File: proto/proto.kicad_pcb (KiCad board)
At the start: 2 copper layers, 12 parts, among them J1 Conn_01x10_Pin, U2 TPIC6595

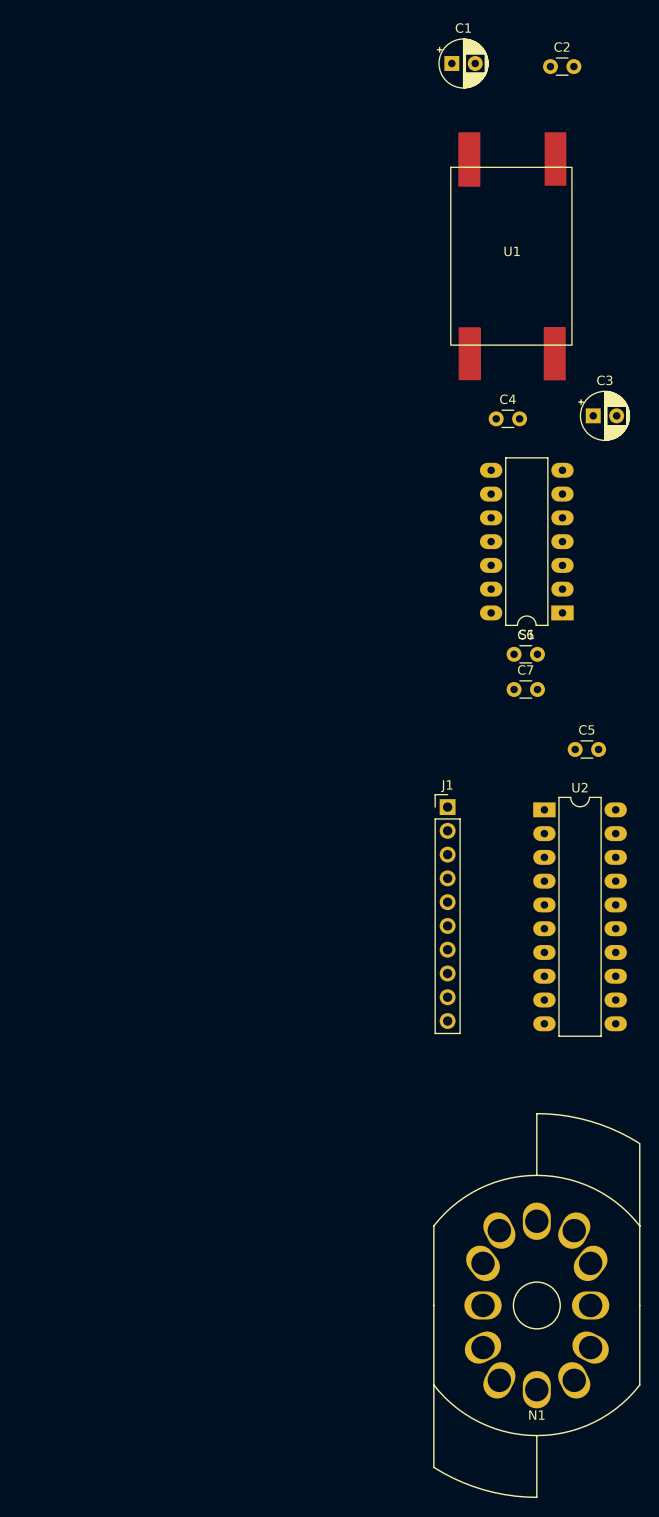
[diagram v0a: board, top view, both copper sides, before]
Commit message: Add footprint for socketed HV supply. Add R1 which was forgotten. Revise layout for significantly better density.
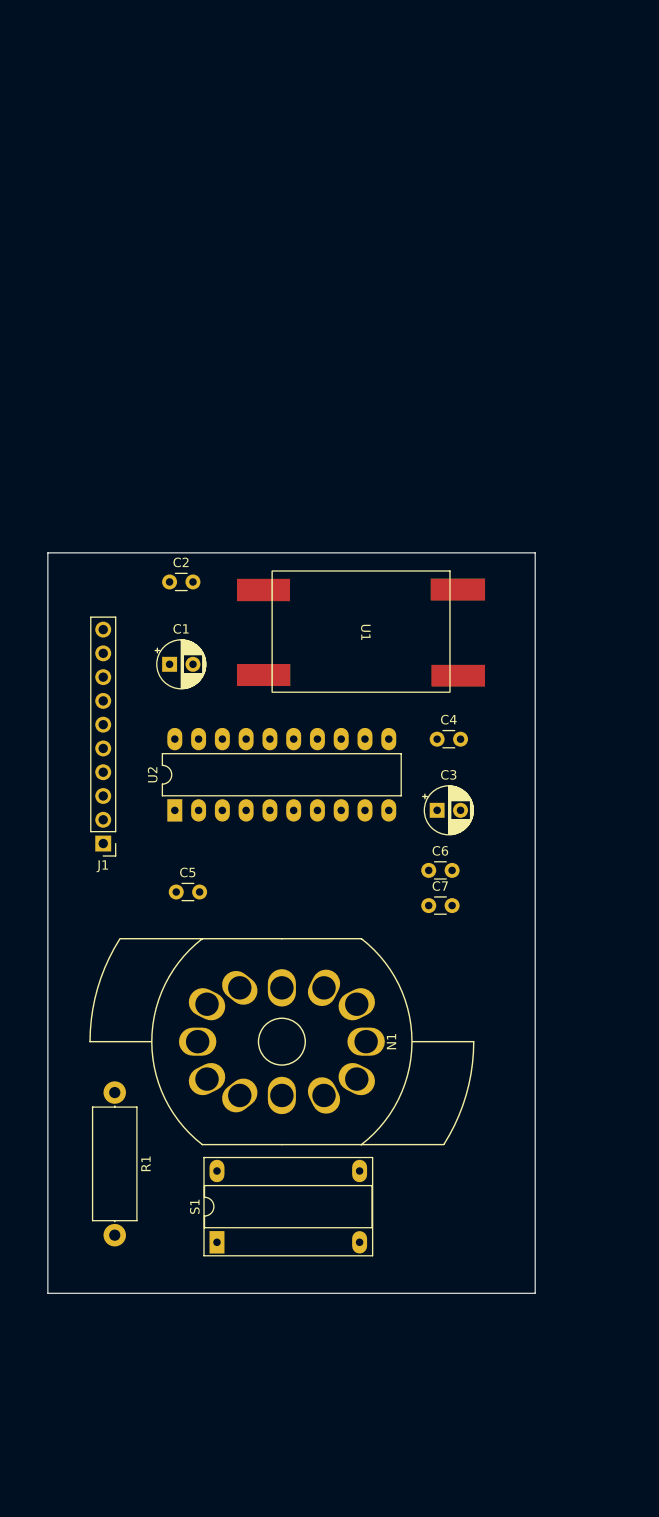
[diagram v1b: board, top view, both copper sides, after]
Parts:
- added R1: R, Resistor_THT:R_Axial_DIN0414_L11.9mm_D4.5mm_P15.24mm_Horizontal, F.Cu at (89.8, 149.2)
- S1: footprint Package_DIP:DIP-14_W7.62mm_LongPads -> NixComp:NCH8200HV_Socket_LongPads
- moved S1 76.7 mm to (100.7, 165.2), turned to 90 degrees
- moved C1 70.9 mm to (95.7, 103.4)
- moved C2 68.5 mm to (95.7, 94.6)
- moved C3 45.3 mm to (124.2, 119.0)
- moved C5 45.3 mm to (96.4, 127.8)
- moved U1 43.3 mm to (116.1, 100.0), turned to -90 degrees
- moved U2 39.5 mm to (96.2, 119.0), turned to 90 degrees
- moved N1 39.2 mm to (107.7, 143.8), turned to 90 degrees
- moved J1 37.0 mm to (88.6, 122.6), turned to 180 degrees
- moved C4 34.8 mm to (124.2, 111.4)
- moved C6 24.8 mm to (123.3, 125.5)
- moved C7 24.8 mm to (123.3, 129.2)
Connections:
- S1 pad 4: Net-(N1-A) -> Net-(S1-HV_OUT)
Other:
- board outline added: 52.1 x 79.1 mm

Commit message: Ongoing development
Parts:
- added J2: Conn_01x05_Pin, Connector_PinHeader_2.54mm:PinHeader_1x05_P2.54mm_Vertical, F.Cu at (132.3, 126.0)
- added J3: Conn_01x05_Pin, Connector_PinHeader_2.54mm:PinHeader_1x05_P2.54mm_Vertical, F.Cu at (84.5, 125.9)
- added J4: Conn_01x05_Pin, Connector_PinHeader_2.54mm:PinHeader_1x05_P2.54mm_Vertical, F.Cu at (129.8, 126.0)
- added J5: Conn_01x05_Pin, Connector_PinHeader_2.54mm:PinHeader_1x05_P2.54mm_Vertical, F.Cu at (87.1, 125.9)
- moved C3 6.54 mm to (129.4, 115.0)
- moved U2 6.30 mm to (102.1, 116.9)
- moved C4 5.78 mm to (129.4, 108.8)
- moved N1 4.47 mm to (111.6, 145.9)
- moved J1 4.11 mm to (92.6, 122.0)
- moved R1 2.68 mm to (89.7, 151.9)
- moved S1 1.85 mm to (100.6, 167.0)
- moved C1 1.43 mm to (96.9, 102.8)
- moved C2 1.26 mm to (96.8, 95.0)
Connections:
- C1 pad 1: Net-(J1-Pin_10) -> Net-(J2-Pin_1)
- C2 pad 1: Net-(J1-Pin_10) -> Net-(J2-Pin_1)
- C3 pad 1: Net-(S1-LV_IN) -> Net-(J5-Pin_1)
- C4 pad 1: Net-(S1-LV_IN) -> Net-(J5-Pin_1)
- C5 pad 1: Net-(J1-Pin_10) -> Net-(J2-Pin_1)
- C6 pad 1: Net-(J1-Pin_10) -> Net-(J5-Pin_1)
- C7 pad 1: Net-(J1-Pin_10) -> Net-(J5-Pin_1)
- J1 pad 10: Net-(J1-Pin_10) -> unconnected-(J1-Pin_10-Pad10)
- J1 pad 2: Net-(J1-Pin_2) -> unconnected-(J1-Pin_2-Pad2)
- J1 pad 5: Net-(J1-Pin_5) -> unconnected-(J1-Pin_5-Pad5)
- J1 pad 6: unconnected-(J1-Pin_6-Pad6) -> Net-(J1-Pin_6)
- J1 pad 7: unconnected-(J1-Pin_7-Pad7) -> Net-(J1-Pin_7)
- J1 pad 9: Net-(J1-Pin_10) -> unconnected-(J1-Pin_9-Pad9)
- S1 pad 1: Net-(S1-LV_IN) -> Net-(J5-Pin_1)
- U1 pad 1: Net-(J1-Pin_10) -> Net-(J2-Pin_1)
- U1 pad 2: Net-(S1-LV_IN) -> Net-(J5-Pin_1)
- U2 pad 12: Net-(J1-Pin_4) -> Net-(J1-Pin_6)
- U2 pad 13: Net-(J1-Pin_2) -> Net-(J1-Pin_3)
- U2 pad 2: Net-(S1-LV_IN) -> Net-(J5-Pin_1)
- U2 pad 8: Net-(J1-Pin_3) -> Net-(J1-Pin_4)
- U2 pad 9: Net-(J1-Pin_5) -> Net-(J1-Pin_7)
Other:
- board size 52.1 x 79.1 mm -> 52.7 x 79.1 mm
- copper layers 2 -> 4

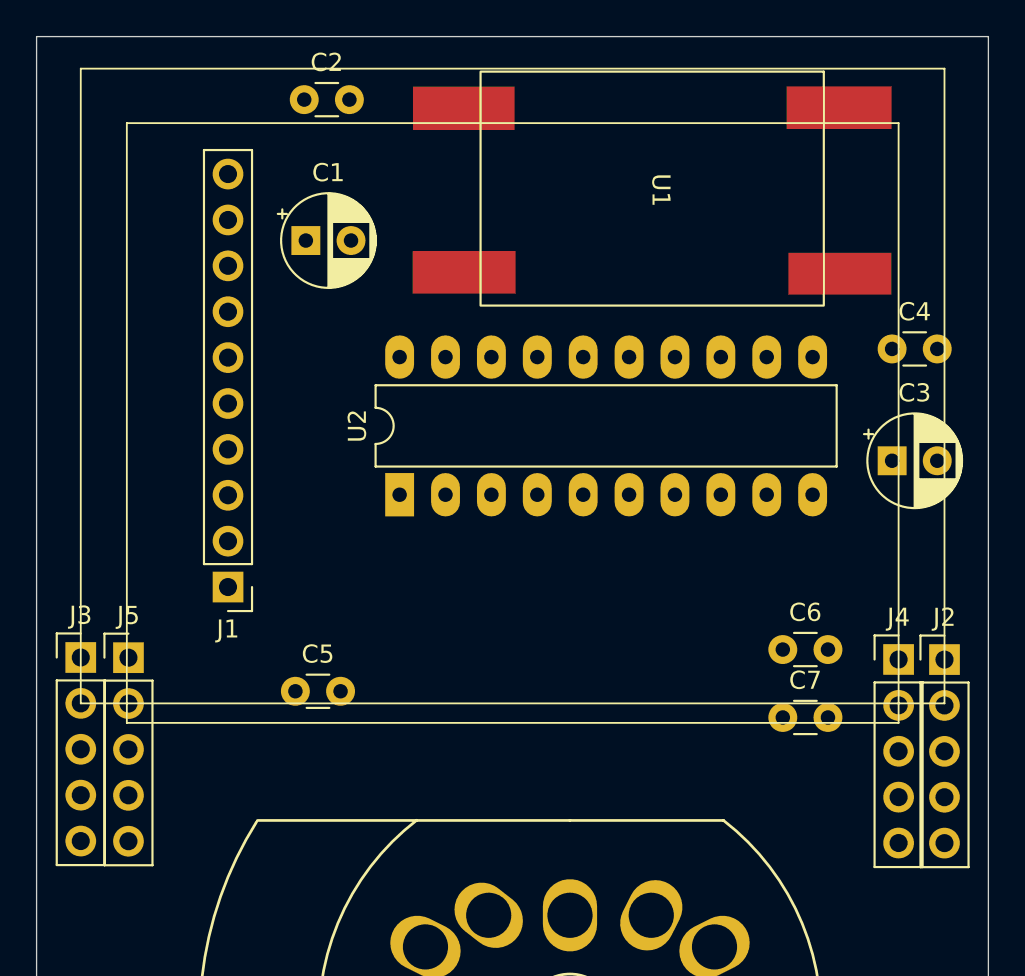
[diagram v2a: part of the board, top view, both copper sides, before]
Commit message: Improve footprint for pin connectors and align four power and ground connectors (I hope)
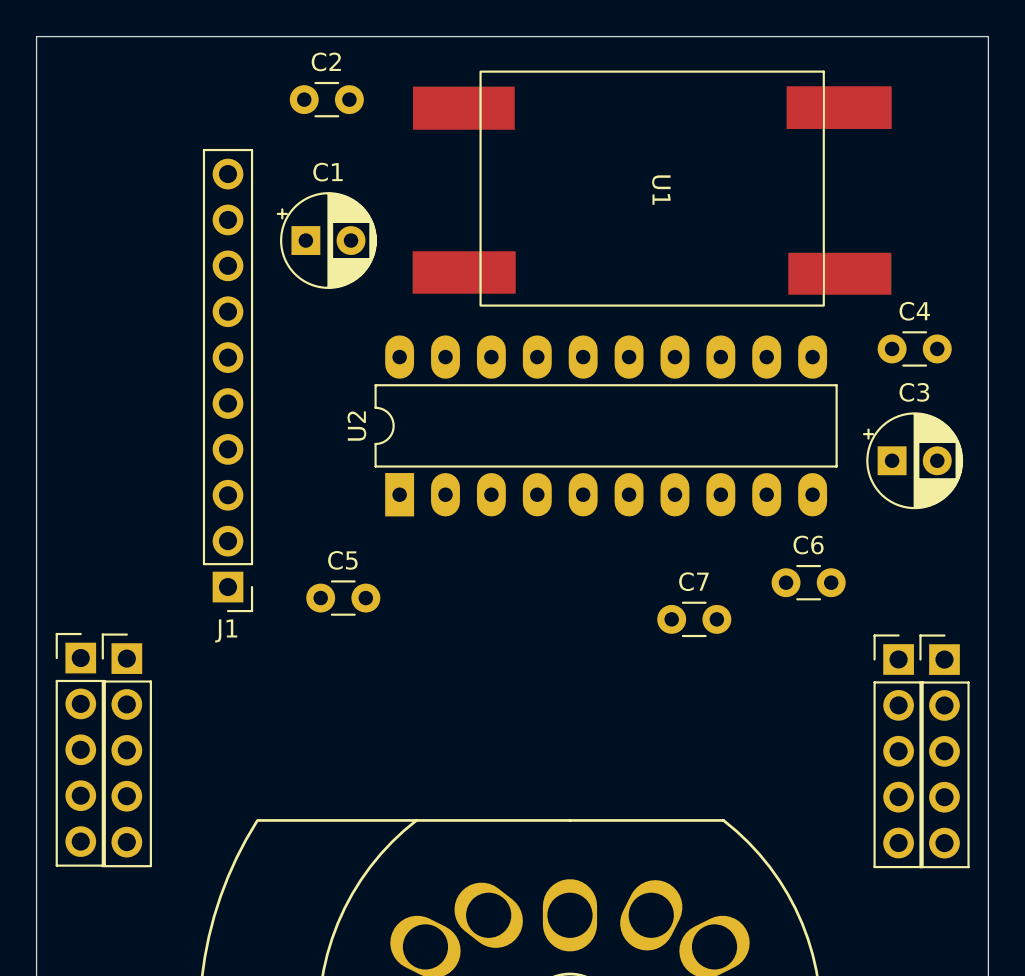
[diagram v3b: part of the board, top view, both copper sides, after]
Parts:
- J2, J3, J4, J5: footprint Connector_PinHeader_2.54mm:PinHeader_1x05_P2.54mm_Vertical -> NixComp:PinHeader_1x05_P2.54mm_Vertical_SmallCourt
- moved C7 8.20 mm to (117.2, 123.8)
- moved C5 5.35 mm to (97.8, 122.6)
- moved C6 3.70 mm to (123.5, 121.8)
- moved J5 0.10 mm to (87.0, 126.0)
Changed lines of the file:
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@@
 		)
 	)
-	(footprint "Connector_PinHeader_2.54mm:PinHeader_1x05_P2.54mm_Vertical"
+	(footprint "NixComp:PinHeader_1x05_P2.54mm_Vertical_SmallCourt"
 		(layer "F.Cu")
 		(at 132.29 126.005)
@@
 		(tags "Through hole pin header THT 1x05 2.54mm single row")
 		(property "Reference" "J2"
-			(at 0 -2.33 0)
+			(at -0.03 -2.43 0)
 			(layer "F.SilkS")
+			(hide yes)
 			(effects
 				(font
@@
 			)
 		)
-		(property "Footprint" "Connector_PinHeader_2.54mm:PinHeader_1x05_P2.54mm_Vertical"
+		(property "Footprint" "NixComp:PinHeader_1x05_P2.54mm_Vertical_SmallCourt"
 			(at 0 0 0)
 			(unlocked yes)
@@
 		)
 		(fp_line
-			(start -1.8 -1.8)
-			(end -1.8 11.95)
-			(stroke
-				(width 0.05)
-				(type solid)
-			)
-			(layer "F.CrtYd")
-		)
-		(fp_line
-			(start -1.8 11.95)
-			(end 1.8 11.95)
-			(stroke
-				(width 0.05)
-				(type solid)
-			)
-			(layer "F.CrtYd")
-		)
-		(fp_line
-			(start 1.8 -1.8)
-			(end -1.8 -1.8)
-			(stroke
-				(width 0.05)
-				(type solid)
-			)
-			(layer "F.CrtYd")
-		)
-		(fp_line
-			(start 1.8 11.95)
-			(end 1.8 -1.8)
-			(stroke
-				(width 0.05)
-				(type solid)
-			)
-			(layer "F.CrtYd")
-		)
-		(fp_line
 			(start -1.27 -0.635)
 			(end -0.635 -1.27)
@@
 	(footprint "Capacitor_THT:C_Disc_D3.0mm_W1.6mm_P2.50mm"
 		(layer "F.Cu")
-		(at 96.36 127.76)
+		(at 97.76 122.6)
 		(descr "C, Disc series, Radial, pin pitch=2.50mm, , diameter*width=3.0*1.6mm^2, Capacitor, http://www.vishay.com/docs/45233/krseries.pdf")
 		(tags "C Disc series Radial pin pitch 2.50mm  diameter 3.0mm width 1.6mm Capacitor")
@@
 	(footprint "Capacitor_THT:C_Disc_D3.0mm_W1.6mm_P2.50mm"
 		(layer "F.Cu")
-		(at 123.34 125.45)
+		(at 123.52 121.75)
 		(descr "C, Disc series, Radial, pin pitch=2.50mm, , diameter*width=3.0*1.6mm^2, Capacitor, http://www.vishay.com/docs/45233/krseries.pdf")
 		(tags "C Disc series Radial pin pitch 2.50mm  diameter 3.0mm width 1.6mm Capacitor")
@@
 		)
 	)
-	(footprint "Connector_PinHeader_2.54mm:PinHeader_1x05_P2.54mm_Vertical"
+	(footprint "NixComp:PinHeader_1x05_P2.54mm_Vertical_SmallCourt"
 		(layer "F.Cu")
 		(at 129.75 126)
@@
 		(tags "Through hole pin header THT 1x05 2.54mm single row")
 		(property "Reference" "J4"
-			(at 0 -2.33 0)
+			(at -0.03 -2.43 0)
 			(layer "F.SilkS")
+			(hide yes)
 			(effects
 				(font
@@
 			)
 		)
-		(property "Footprint" "Connector_PinHeader_2.54mm:PinHeader_1x05_P2.54mm_Vertical"
+		(property "Footprint" "NixComp:PinHeader_1x05_P2.54mm_Vertical_SmallCourt"
 			(at 0 0 0)
 			(unlocked yes)
@@
 		)
 		(fp_line
-			(start -1.8 -1.8)
-			(end -1.8 11.95)
-			(stroke
-				(width 0.05)
-				(type solid)
-			)
-			(layer "F.CrtYd")
-		)
-		(fp_line
-			(start -1.8 11.95)
-			(end 1.8 11.95)
-			(stroke
-				(width 0.05)
-				(type solid)
-			)
-			(layer "F.CrtYd")
-		)
-		(fp_line
-			(start 1.8 -1.8)
-			(end -1.8 -1.8)
-			(stroke
-				(width 0.05)
-				(type solid)
-			)
-			(layer "F.CrtYd")
-		)
-		(fp_line
-			(start 1.8 11.95)
-			(end 1.8 -1.8)
-			(stroke
-				(width 0.05)
-				(type solid)
-			)
-			(layer "F.CrtYd")
-		)
-		(fp_line
 			(start -1.27 -0.635)
 			(end -0.635 -1.27)
@@
 		)
 	)
-	(footprint "Connector_PinHeader_2.54mm:PinHeader_1x05_P2.54mm_Vertical"
+	(footprint "NixComp:PinHeader_1x05_P2.54mm_Vertical_SmallCourt"
 		(layer "F.Cu")
-		(at 87.12 125.9)
+		(at 87.03 125.95)
 		(descr "Through hole straight pin header, 1x05, 2.54mm pitch, single row")
 		(tags "Through hole pin header THT 1x05 2.54mm single row")
 		(property "Reference" "J5"
-			(at 0 -2.33 0)
+			(at -0.03 -2.43 0)
 			(layer "F.SilkS")
+			(hide yes)
 			(effects
 				(font
@@
 			)
 		)
-		(property "Footprint" "Connector_PinHeader_2.54mm:PinHeader_1x05_P2.54mm_Vertical"
+		(property "Footprint" "NixComp:PinHeader_1x05_P2.54mm_Vertical_SmallCourt"
 			(at 0 0 0)
 			(unlocked yes)
@@
 		)
 		(fp_line
-			(start -1.8 -1.8)
-			(end -1.8 11.95)
-			(stroke
-				(width 0.05)
-				(type solid)
-			)
-			(layer "F.CrtYd")
-		)
-		(fp_line
-			(start -1.8 11.95)
-			(end 1.8 11.95)
-			(stroke
-				(width 0.05)
-				(type solid)
-			)
-			(layer "F.CrtYd")
-		)
-		(fp_line
-			(start 1.8 -1.8)
-			(end -1.8 -1.8)
-			(stroke
-				(width 0.05)
-				(type solid)
-			)
-			(layer "F.CrtYd")
-		)
-		(fp_line
-			(start 1.8 11.95)
-			(end 1.8 -1.8)
-			(stroke
-				(width 0.05)
-				(type solid)
-			)
-			(layer "F.CrtYd")
-		)
-		(fp_line
 			(start -1.27 -0.635)
 			(end -0.635 -1.27)
@@
 	(footprint "Capacitor_THT:C_Disc_D3.0mm_W1.6mm_P2.50mm"
 		(layer "F.Cu")
-		(at 123.34 129.21)
+		(at 117.19 123.78)
 		(descr "C, Disc series, Radial, pin pitch=2.50mm, , diameter*width=3.0*1.6mm^2, Capacitor, http://www.vishay.com/docs/45233/krseries.pdf")
 		(tags "C Disc series Radial pin pitch 2.50mm  diameter 3.0mm width 1.6mm Capacitor")
@@
 		)
 	)
-	(footprint "Connector_PinHeader_2.54mm:PinHeader_1x05_P2.54mm_Vertical"
+	(footprint "NixComp:PinHeader_1x05_P2.54mm_Vertical_SmallCourt"
 		(layer "F.Cu")
-		(at 84.48 125.89)
+		(at 84.48 125.92)
 		(descr "Through hole straight pin header, 1x05, 2.54mm pitch, single row")
 		(tags "Through hole pin header THT 1x05 2.54mm single row")
 		(property "Reference" "J3"
-			(at 0 -2.33 0)
+			(at -0.03 -2.43 0)
 			(layer "F.SilkS")
+			(hide yes)
 			(effects
 				(font
@@
 			)
 		)
-		(property "Footprint" "Connector_PinHeader_2.54mm:PinHeader_1x05_P2.54mm_Vertical"
+		(property "Footprint" "NixComp:PinHeader_1x05_P2.54mm_Vertical_SmallCourt"
 			(at 0 0 0)
 			(unlocked yes)
@@
 		)
 		(fp_line
-			(start -1.8 -1.8)
-			(end -1.8 11.95)
-			(stroke
-				(width 0.05)
-				(type solid)
-			)
-			(layer "F.CrtYd")
-		)
-		(fp_line
-			(start -1.8 11.95)
-			(end 1.8 11.95)
-			(stroke
-				(width 0.05)
-				(type solid)
-			)
-			(layer "F.CrtYd")
-		)
-		(fp_line
-			(start 1.8 -1.8)
-			(end -1.8 -1.8)
-			(stroke
-				(width 0.05)
-				(type solid)
-			)
-			(layer "F.CrtYd")
-		)
-		(fp_line
-			(start 1.8 11.95)
-			(end 1.8 -1.8)
-			(stroke
-				(width 0.05)
-				(type solid)
-			)
-			(layer "F.CrtYd")
-		)
-		(fp_line
 			(start -1.27 -0.635)
 			(end -0.635 -1.27)
@@
 	)
 	(gr_rect
-		(start 87.03 96.31)
-		(end 129.75 129.51)
-		(stroke
-			(width 0.1)
-			(type default)
-		)
-		(fill none)
-		(layer "F.SilkS")
-	)
-	(gr_rect
-		(start 84.48 93.2946)
-		(end 132.29 128.43)
-		(stroke
-			(width 0.1)
-			(type default)
-		)
-		(fill none)
-		(layer "F.SilkS")
-	)
-	(gr_rect
 		(start 82.033846 91.52)
 		(end 134.72 170.643846)
@@
 		(layer "F.SilkS")
 		(pts
-			(xy 132.29 129.59) (xy 129.75 129.59)
-		)
-		(height 0)
-		(gr_text "2.5400 mm"
-			(at 131.02 128.49 0)
-			(layer "F.SilkS")
-			(effects
-				(font
-					(size 1 1)
-					(thickness 0.1)
-				)
-			)
-		)
-		(format
-			(prefix "")
-			(suffix "")
-			(units 3)
-			(units_format 1)
-			(precision 4)
-		)
-		(style
-			(thickness 0.1)
-			(arrow_length 1.27)
-			(text_position_mode 0)
-			(extension_height 0.58642)
-			(extension_offset 0.5) keep_text_aligned)
-	)
-	(dimension
-		(type aligned)
-		(layer "F.SilkS")
-		(pts
 			(xy 108.39 131.081923) (xy 82.06 131.081923)
 		)
@@
 		(layer "F.SilkS")
 		(pts
-			(xy 84.48 129.51) (xy 87.03 129.51)
+			(xy 87.03 126.92) (xy 129.74 126.92)
 		)
 		(height 0)
-		(gr_text "2.5500 mm"
-			(at 85.755 128.41 0)
+		(gr_text "42.7100 mm"
+			(at 108.385 125.82 0)
 			(layer "F.SilkS")
 			(effects

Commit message: Ongoing development. Add ground vias.
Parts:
- J1: value Conn_01x10_Pin -> J1; footprint Connector_PinHeader_2.54mm:PinHeader_1x10_P2.54mm_Vertical -> NixComp:PinHeader_1x05_P2.54mm_Vertical_SmallCourt
- J2: value Conn_01x05_Pin -> J2
- J4: value Conn_01x05_Pin -> J4
- moved J1 15.8 mm to (93.9, 106.2), turned to 0 degrees
- moved C1 10.8 mm to (86.2, 101.3)
- moved C2 10.6 mm to (86.3, 94.8)
- moved U1 3.41 mm to (112.7, 100.3)
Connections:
- J1 pad 2: unconnected-(J1-Pin_2-Pad2) -> Net-(J1-Pin_2)
- J1 pad 5: unconnected-(J1-Pin_5-Pad5) -> Net-(J1-Pin_5)
- U2 pad 12: Net-(J1-Pin_6) -> Net-(J1-Pin_4)
- U2 pad 13: Net-(J1-Pin_3) -> Net-(J1-Pin_2)
- U2 pad 8: Net-(J1-Pin_4) -> Net-(J1-Pin_3)
- U2 pad 9: Net-(J1-Pin_7) -> Net-(J1-Pin_5)
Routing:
- net GND: track 0.00 -> 48.8 mm, vias 0 -> 24
- added copper zone on In1.Cu, net GND
- added copper zone on In2.Cu, net GND

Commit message: Equivalent of code complete on the proto board
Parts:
- J3: value Conn_01x05_Pin -> J3
- J5: value Conn_01x05_Pin -> J5
- moved C2 65.3 mm to (132.3, 141.2), turned to 180 degrees
- moved C4 41.1 mm to (89.5, 99.0), turned to -90 degrees
- moved C1 39.8 mm to (126.0, 99.2), turned to -90 degrees
- moved C5 39.4 mm to (130.0, 99.9), turned to -90 degrees
- moved C6 36.5 mm to (87.1, 122.7), turned to 90 degrees
- moved C3 34.1 mm to (99.2, 99.1), turned to -90 degrees
- moved J1 32.3 mm to (126.1, 109.1)
- moved C7 17.1 mm to (100.4, 120.2), turned to 180 degrees
- moved U2 4.25 mm to (97.9, 117.4)
- moved R1 3.91 mm to (91.8, 148.6)
- moved N1 2.19 mm to (109.4, 145.6)
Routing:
- net Net-(J5-Pin_1): track 0.00 -> 158.8 mm
- net GND: track 48.8 -> 200.3 mm, vias 24 -> 40
- net Net-(J2-Pin_1): track 0.00 -> 62.1 mm
- net Net-(N1-D5): track 0.00 -> 48.8 mm
- net Net-(N1-D2): track 0.00 -> 46.5 mm
- net Net-(N1-D7): track 0.00 -> 45.3 mm
- net Net-(N1-D4): track 0.00 -> 43.5 mm
- net Net-(N1-D6): track 0.00 -> 42.9 mm
- net Net-(N1-D3): track 0.00 -> 36.4 mm
- net Net-(N1-D1): track 0.00 -> 34.9 mm
- net Net-(J1-Pin_1): track 0.00 -> 31.9 mm
- net Net-(N1-D0): track 0.00 -> 22.7 mm
- net Net-(N1-A): track 0.00 -> 14.3 mm
- net Net-(J1-Pin_4): track 0.00 -> 14.3 mm
- net Net-(J1-Pin_2): track 0.00 -> 12.5 mm
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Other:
- board size 52.7 x 79.1 mm -> 57.7 x 79.1 mm

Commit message: Completely revise high voltage converter footprint and circuit du to previous errors. Generate Gerbers. Some issues remain.
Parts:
- S1: value ~ -> NCH8200HV; footprint NixComp:NCH8200HV_Socket_LongPads -> NixComp:NCH8200HV
- moved S1 8.94 mm to (109.4, 165.3), turned to 0 degrees
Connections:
- S1 pad 1: Net-(J5-Pin_1) -> Net-(S1-HV_OUT)
- S1 pad 2: GND -> Net-(J5-Pin_1)
- S1 pad 4: Net-(S1-HV_OUT) -> GND
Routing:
- net GND: track 200.3 -> 231.1 mm, vias 40 -> 24
- net Net-(J5-Pin_1): track 158.8 -> 167.7 mm
- net Net-(N1-D3): track 36.4 -> 38.4 mm
- net Net-(N1-D4): track 43.5 -> 44.3 mm
- net Net-(S1-HV_OUT): track 10.6 -> 11.4 mm
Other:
- board size 57.7 x 79.1 mm -> 57.7 x 90 mm
